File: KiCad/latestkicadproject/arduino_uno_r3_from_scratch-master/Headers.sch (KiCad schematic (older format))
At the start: 4 parts, among them P1 Power Header, P2 Analog Header, P3 Digital Header 02, P4 Digital Header 01

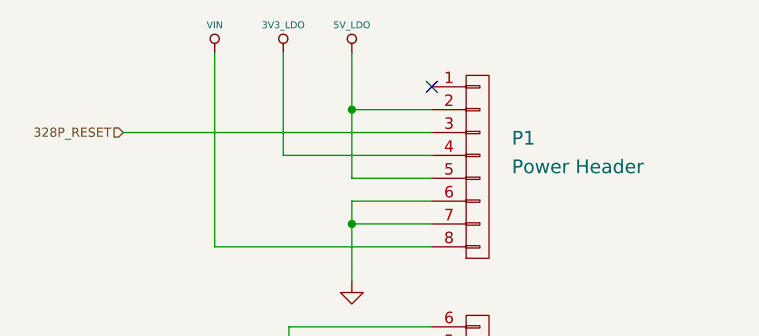
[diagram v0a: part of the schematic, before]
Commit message: 28feb
Aanpassing KiCad+deel footprints
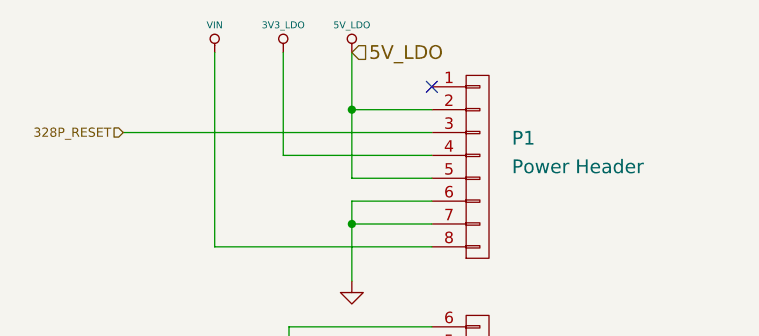
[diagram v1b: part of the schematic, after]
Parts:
- P1, P2, P3, P4: footprint ~ -> (none)
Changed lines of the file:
@@
 F 0 "P1" H 6400 2500 60  0000 L CNN
 F 1 "Power Header" H 6400 2375 60  0000 L CNN
-F 2 "~" H 6250 2375 60  0000 C CNN
+F 2 "" H 6250 2375 60  0000 C CNN
 F 3 "http://sullinscorp.com/catalogs/101_PAGE114-115_.100_FEMALE_HDR.pdf" H 6250 2375 60  0001 C CNN
 F 4 "Connector Header 8 Position 0.100\" (2.54mm) Gold Surface Mount" H 6250 2375 60  0001 C CNN "Characteristics"
@@
 F 0 "P3" H 6450 4250 60  0000 C CNN
 F 1 "Digital Header 02" H 6400 4375 60  0000 L CNN
-F 2 "~" H 6250 4375 60  0000 C CNN
+F 2 "" H 6250 4375 60  0000 C CNN
 F 3 "http://sullinscorp.com/catalogs/101_PAGE114-115_.100_FEMALE_HDR.pdf" H 6250 4375 60  0001 C CNN
 F 4 "Connector Header 10 Position 0.100\" (2.54mm) Gold Surface Mount" H 6250 4375 60  0001 C CNN "Characteristics"
@@
 F 0 "P2" H 6400 3200 60  0000 L CNN
 F 1 "Analog Header" H 6400 3325 60  0000 L CNN
-F 2 "~" H 6250 3325 60  0000 C CNN
+F 2 "" H 6250 3325 60  0000 C CNN
 F 3 "http://sullinscorp.com/catalogs/101_PAGE114-115_.100_FEMALE_HDR.pdf" H 6250 3325 60  0001 C CNN
 F 4 "Connector Header 6 Position 0.100\" (2.54mm) Gold Surface Mount" H 6250 3325 60  0001 C CNN "Characteristics"
@@
 F 0 "P4" H 6400 5650 60  0000 L CNN
 F 1 "Digital Header 01" H 6400 5525 60  0000 L CNN
-F 2 "~" H 6250 5525 60  0000 C CNN
+F 2 "" H 6250 5525 60  0000 C CNN
 F 3 "http://sullinscorp.com/catalogs/101_PAGE114-115_.100_FEMALE_HDR.pdf" H 6250 5525 60  0001 C CNN
 F 4 "Connector Header 8 Position 0.100\" (2.54mm) Gold Surface Mount" H 6250 5525 60  0001 C CNN "Characteristics"
@@
 	1    0    0    -1
 $EndComp
+Text HLabel 5700 1875 2    60   Input ~ 0
+5V_LDO
 $EndSCHEMATC

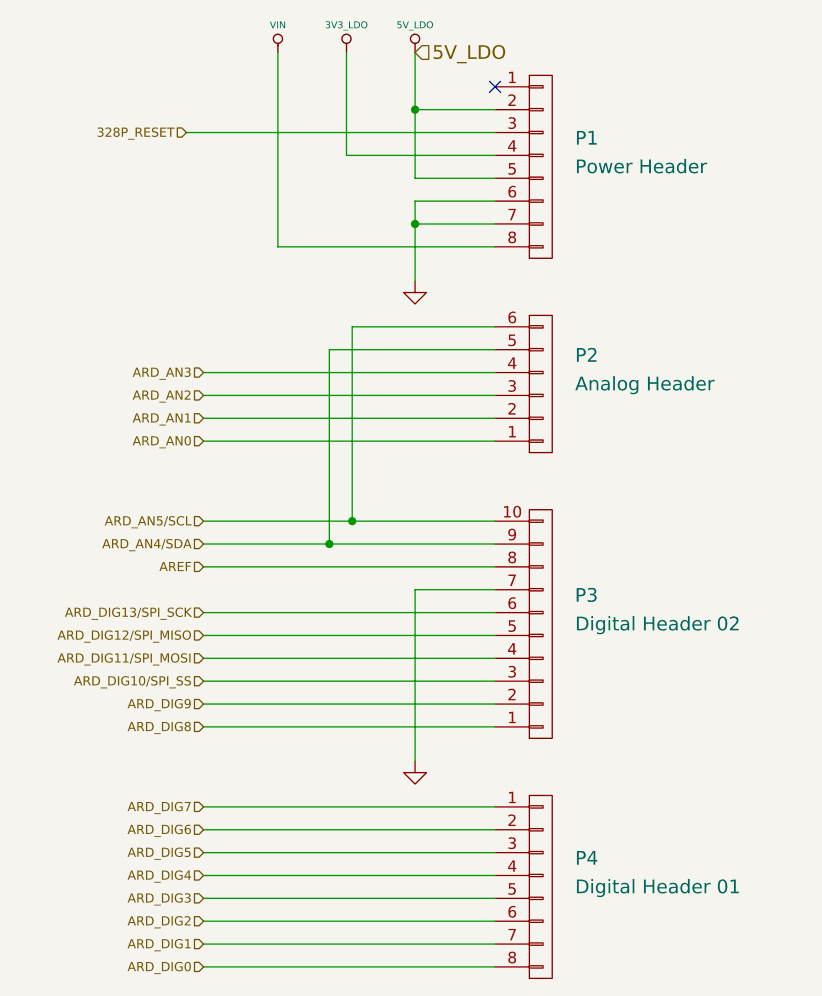
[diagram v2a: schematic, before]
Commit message: Aanpassing KiCad PCB ontwerp + footprints
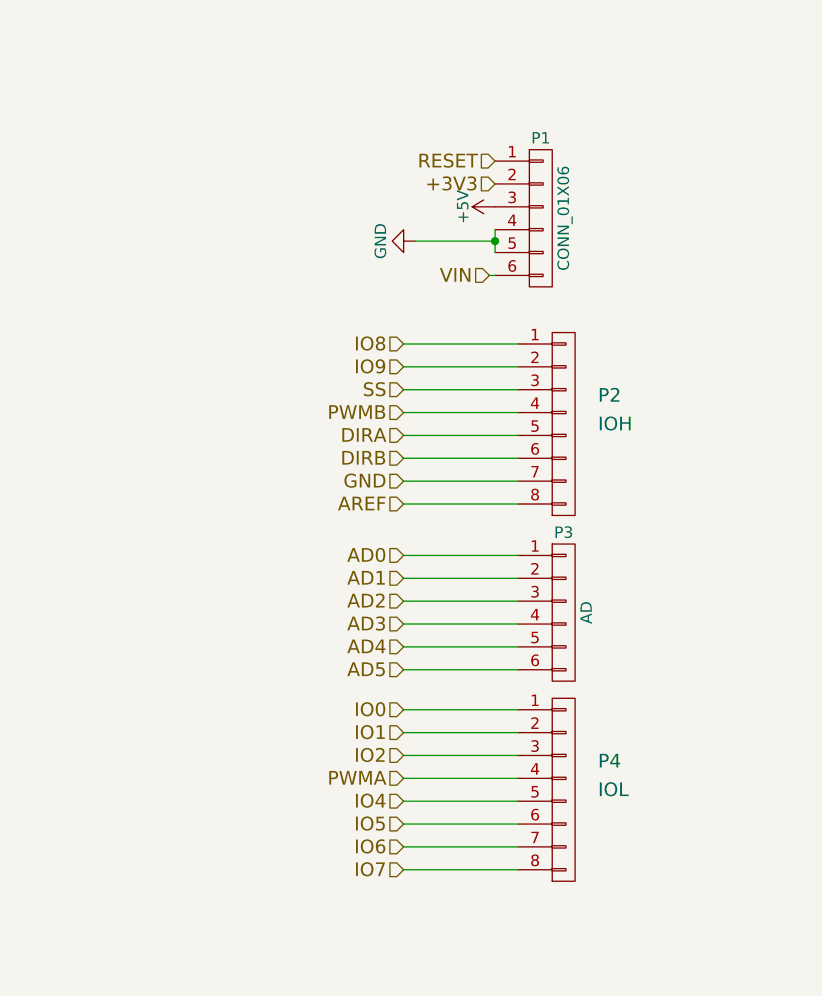
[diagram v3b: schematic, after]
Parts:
- removed P1: Power Header, symbol CONN_01X08
- removed P2: Analog Header, symbol CONN_01X06
- removed P3: Digital Header 02, symbol CONN_01X10
- added P1: CONN_01X06, Pin_Headers:Pin_Header_Straight_1x06_Pitch2.00mm, symbol CONN_01X06
- added P2: IOH, Pin_Headers:Pin_Header_Straight_1x08_Pitch2.00mm, symbol CONN_01X08
- added P3: AD, Pin_Headers:Pin_Header_Straight_1x06_Pitch2.00mm, symbol CONN_01X06
- P4: value Digital Header 01 -> IOL; footprint (none) -> Pin_Headers:Pin_Header_Straight_1x08_Pitch2.00mm
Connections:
- net AREF: now also P2.8 (P8)
- net ARD_DIG0 renamed IO7
- net ARD_DIG1 renamed IO6
- net ARD_DIG2 renamed IO5
- net ARD_DIG3 renamed IO4
- net ARD_DIG4 renamed PWMA
- net ARD_DIG5 renamed IO2
- net ARD_DIG6 renamed IO1
- net ARD_DIG7 renamed IO0
- new net +3V3: P1.2 (P2)
- new net +5V: P1.3 (P3)
- new net AD0: P3.1 (P1)
- new net AD1: P3.2 (P2)
- new net AD2: P3.3 (P3)
- new net AD3: P3.4 (P4)
- new net AD4: P3.5 (P5)
- new net AD5: P3.6 (P6)
- new net DIRA: P2.5 (P5)
- new net DIRB: P2.6 (P6)
- new net GND: P1.4 (P4), P1.5 (P5), P2.7 (P7)
- new net IO8: P2.1 (P1)
- new net IO9: P2.2 (P2)
- new net PWMB: P2.4 (P4)
- new net RESET: P1.1 (P1)
- new net SS: P2.3 (P3)
- new net VIN: P1.6 (P6)
- no-connect marks 1 -> 0
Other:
- moved on the sheet: P4

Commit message: pcb routing
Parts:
- P1, P3: footprint Pin_Headers:Pin_Header_Straight_1x06_Pitch2.00mm -> Pin_Headers:Pin_Header_Straight_1x06_Pitch2.54mm
- P2: footprint Pin_Headers:Pin_Header_Straight_1x08_Pitch2.00mm -> Pin_Headers:Pin_Header_Straight_1x08_Pitch2.54mm
- P4: value IOL -> H4; footprint Pin_Headers:Pin_Header_Straight_1x08_Pitch2.00mm -> Pin_Headers:Pin_Header_Straight_1x08_Pitch2.54mm
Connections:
- net +5V: now also P1.5 (P5); no longer P1.3 (P3)
- net AD0: now also P2.8 (P8); no longer P3.1 (P1)
- net AD1: now also P2.7 (P7); no longer P3.2 (P2)
- net AD2: now also P2.6 (P6); no longer P3.3 (P3)
- net AD3: now also P2.5 (P5); no longer P3.4 (P4)
- net AD4: now also P2.4 (P4); no longer P3.5 (P5)
- net AD5: now also P2.3 (P3); no longer P3.6 (P6)
- net AREF: now also P1.4 (P4); no longer P2.8 (P8)
- net DIRA: now also P4.8 (P8); no longer P2.5 (P5)
- net DIRB: now also P1.6 (P6); no longer P2.6 (P6)
- net GND: now also P1.3 (P3), P3.5 (P5), P3.6 (P6); no longer P1.4 (P4), P1.5 (P5), P2.7 (P7)
- net IO0: now also P2.1 (P1); no longer P4.1 (P1)
- net IO1: now also P3.1 (P1); no longer P4.2 (P2)
- net IO2: now also P3.2 (P2); no longer P4.3 (P3)
- net IO4: now also P3.4 (P4); no longer P4.5 (P5)
- net IO5: now also P4.1 (P1); no longer P4.6 (P6)
- net IO6: now also P4.2 (P2); no longer P4.7 (P7)
- net IO7: now also P4.3 (P3); no longer P4.8 (P8)
- net IO8: now also P4.4 (P4); no longer P2.1 (P1)
- net IO9: now also P4.5 (P5); no longer P2.2 (P2)
- net PWMA: now also P3.3 (P3); no longer P4.4 (P4)
- net PWMB: now also P4.7 (P7); no longer P2.4 (P4)
- net RESET: now also P2.2 (P2); no longer P1.1 (P1)
- net SS: now also P4.6 (P6); no longer P2.3 (P3)
- net VIN: now also P1.1 (P1); no longer P1.6 (P6)
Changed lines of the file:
@@
 LIBS:LP2985-33DBVR
 LIBS:degson
+LIBS:PHT6NQ10T_135
 EELAYER 25 0
 EELAYER END
@@
 P 6350 5100
 F 0 "P4" H 6500 5225 60  0000 L CNN
-F 1 "IOL" H 6500 5100 60  0000 L CNN
-F 2 "Pin_Headers:Pin_Header_Straight_1x08_Pitch2.00mm" H 6350 5100 60  0001 C CNN
+F 1 "H4" H 6500 5100 60  0000 L CNN
+F 2 "Pin_Headers:Pin_Header_Straight_1x08_Pitch2.54mm" H 6350 5100 60  0001 C CNN
 F 3 "http://sullinscorp.com/catalogs/101_PAGE114-115_.100_FEMALE_HDR.pdf" H 6350 5100 60  0001 C CNN
 F 4 "Connector Header 8 Position 0.100\" (2.54mm) Gold Surface Mount" H 6350 5100 60  0001 C CNN "Characteristics"
@@
 Text HLabel 6050 2450 0    60   Input ~ 0
 +3V3
-Text HLabel 6025 2850 0    60   Input ~ 0
+Text HLabel 6050 2350 0    60   Input ~ 0
 VIN
-Text HLabel 6050 2350 0    60   Input ~ 0
+Text HLabel 5650 3250 0    60   Input ~ 0
 RESET
 $Comp
@@
 F 0 "P1" H 6250 2950 50  0000 C CNN
 F 1 "CONN_01X06" V 6350 2600 50  0000 C CNN
-F 2 "Pin_Headers:Pin_Header_Straight_1x06_Pitch2.00mm" H 6250 2600 60  0001 C CNN
+F 2 "Pin_Headers:Pin_Header_Straight_1x06_Pitch2.54mm" H 6250 2600 60  0001 C CNN
 F 3 "" H 6250 2600 60  0000 C CNN
 	1    6250 2600
@@
 L +5V #PWR09
 U 1 1 5AA11396
+P 6050 2750
+F 0 "#PWR09" H 6050 2600 50  0001 C CNN
+F 1 "+5V" H 6050 2890 50  0000 C CNN
+F 2 "" H 6050 2750 50  0001 C CNN
+F 3 "" H 6050 2750 50  0001 C CNN
+	1    6050 2750
+	0    -1   -1   0
+$EndComp
+$Comp
+L GND #PWR010
+U 1 1 5AA115CD
 P 6050 2550
-F 0 "#PWR09" H 6050 2400 50  0001 C CNN
-F 1 "+5V" H 6050 2690 50  0000 C CNN
+F 0 "#PWR010" H 6050 2300 50  0001 C CNN
+F 1 "GND" H 6050 2400 50  0000 C CNN
 F 2 "" H 6050 2550 50  0001 C CNN
 F 3 "" H 6050 2550 50  0001 C CNN
 	1    6050 2550
-	0    -1   -1   0
-$EndComp
-Wire Wire Line
-	6050 2750 6050 2650
-Wire Wire Line
-	6050 2700 5700 2700
-Connection ~ 6050 2700
-$Comp
-L GND #PWR010
-U 1 1 5AA115CD
-P 5700 2700
-F 0 "#PWR010" H 5700 2450 50  0001 C CNN
-F 1 "GND" H 5700 2550 50  0000 C CNN
-F 2 "" H 5700 2700 50  0001 C CNN
-F 3 "" H 5700 2700 50  0001 C CNN
-	1    5700 2700
 	0    1    1    0
 $EndComp
@@
 F 0 "P2" H 6500 3625 60  0000 L CNN
 F 1 "IOH" H 6500 3500 60  0000 L CNN
-F 2 "Pin_Headers:Pin_Header_Straight_1x08_Pitch2.00mm" H 6350 3500 60  0001 C CNN
+F 2 "Pin_Headers:Pin_Header_Straight_1x08_Pitch2.54mm" H 6350 3500 60  0001 C CNN
 F 3 "http://sullinscorp.com/catalogs/101_PAGE114-115_.100_FEMALE_HDR.pdf" H 6350 3500 60  0001 C CNN
 F 4 "Connector Header 8 Position 0.100\" (2.54mm) Gold Surface Mount" H 6350 3500 60  0001 C CNN "Characteristics"
@@
 F 0 "P3" H 6350 4675 50  0000 C CNN
 F 1 "AD" V 6450 4325 50  0000 C CNN
-F 2 "Pin_Headers:Pin_Header_Straight_1x06_Pitch2.00mm" H 6350 4325 60  0001 C CNN
+F 2 "Pin_Headers:Pin_Header_Straight_1x06_Pitch2.54mm" H 6350 4325 60  0001 C CNN
 F 3 "" H 6350 4325 60  0000 C CNN
 	1    6350 4325
@@
 Wire Wire Line
 	6150 5450 5650 5450
+Text HLabel 5650 5050 0    60   Input ~ 0
+IO8
+Text HLabel 5650 5150 0    60   Input ~ 0
+IO9
+Text HLabel 5650 5250 0    60   Input ~ 0
+SS
+Text HLabel 5650 5350 0    60   Input ~ 0
+PWMB
+Text HLabel 5650 5450 0    60   Input ~ 0
+DIRA
+Text HLabel 6025 2850 0    60   Input ~ 0
+DIRB
+Text HLabel 5650 4475 0    60   Input ~ 0
+GND
+Text HLabel 6050 2650 0    60   Input ~ 0
+AREF
+Text HLabel 5650 3850 0    60   Input ~ 0
+AD0
+Text HLabel 5650 3750 0    60   Input ~ 0
+AD1
+Text HLabel 5650 3650 0    60   Input ~ 0
+AD2
+Text HLabel 5650 3550 0    60   Input ~ 0
+AD3
+Text HLabel 5650 3450 0    60   Input ~ 0
+AD4
+Text HLabel 5650 3350 0    60   Input ~ 0
+AD5
+Text HLabel 5650 4075 0    60   Input ~ 0
+IO1
 Text HLabel 5650 3150 0    60   Input ~ 0
-IO8
-Text HLabel 5650 3250 0    60   Input ~ 0
-IO9
-Text HLabel 5650 3350 0    60   Input ~ 0
-SS
-Text HLabel 5650 3450 0    60   Input ~ 0
-PWMB
-Text HLabel 5650 3550 0    60   Input ~ 0
-DIRA
-Text HLabel 5650 3650 0    60   Input ~ 0
-DIRB
-Text HLabel 5650 3750 0    60   Input ~ 0
+IO0
+Text HLabel 5650 4175 0    60   Input ~ 0
+IO2
+Text HLabel 5650 4275 0    60   Input ~ 0
+PWMA
+Text HLabel 5650 4375 0    60   Input ~ 0
+IO4
+Text HLabel 5650 4750 0    60   Input ~ 0
+IO5
+Text HLabel 5650 4850 0    60   Input ~ 0
+IO6
+Text HLabel 5650 4950 0    60   Input ~ 0
+IO7
+Wire Wire Line
+	6025 2850 6050 2850
+Text HLabel 5650 4575 0    60   Input ~ 0
 GND
-Text HLabel 5650 3850 0    60   Input ~ 0
-AREF
-Text HLabel 5650 4075 0    60   Input ~ 0
-AD0
-Text HLabel 5650 4175 0    60   Input ~ 0
-AD1
-Text HLabel 5650 4275 0    60   Input ~ 0
-AD2
-Text HLabel 5650 4375 0    60   Input ~ 0
-AD3
-Text HLabel 5650 4475 0    60   Input ~ 0
-AD4
-Text HLabel 5650 4575 0    60   Input ~ 0
-AD5
-Text HLabel 5650 4850 0    60   Input ~ 0
-IO1
-Text HLabel 5650 4750 0    60   Input ~ 0
-IO0
-Text HLabel 5650 4950 0    60   Input ~ 0
-IO2
-Text HLabel 5650 5050 0    60   Input ~ 0
-PWMA
-Text HLabel 5650 5150 0    60   Input ~ 0
-IO4
-Text HLabel 5650 5250 0    60   Input ~ 0
-IO5
-Text HLabel 5650 5350 0    60   Input ~ 0
-IO6
-Text HLabel 5650 5450 0    60   Input ~ 0
-IO7
-Wire Wire Line
-	6025 2850 6050 2850
 $EndSCHEMATC

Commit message: PCB routing v1
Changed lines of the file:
@@
 LIBS:degson
 LIBS:PHT6NQ10T_135
+LIBS:L298P
 EELAYER 25 0
 EELAYER END
@@
 Text HLabel 6025 2850 0    60   Input ~ 0
 DIRB
-Text HLabel 5650 4475 0    60   Input ~ 0
-GND
 Text HLabel 6050 2650 0    60   Input ~ 0
 AREF
@@
 Wire Wire Line
 	6025 2850 6050 2850
-Text HLabel 5650 4575 0    60   Input ~ 0
+$Comp
+L GND #PWR011
+U 1 1 5AB3A500
+P 5650 4575
+F 0 "#PWR011" H 5650 4325 50  0001 C CNN
+F 1 "GND" H 5650 4425 50  0000 C CNN
+F 2 "" H 5650 4575 50  0001 C CNN
+F 3 "" H 5650 4575 50  0001 C CNN
+	1    5650 4575
+	1    0    0    -1
+$EndComp
+$Comp
+L GND #PWR012
+U 1 1 5AB3A534
+P 5650 4475
+F 0 "#PWR012" H 5650 4225 50  0001 C CNN
+F 1 "GND" H 5650 4325 50  0000 C CNN
+F 2 "" H 5650 4475 50  0001 C CNN
+F 3 "" H 5650 4475 50  0001 C CNN
+	1    5650 4475
+	1    0    0    -1
+$EndComp
+Text HLabel 5050 2500 0    60   Input ~ 0
 GND
+$Comp
+L GND #PWR013
+U 1 1 5AB75FDA
+P 5050 2500
+F 0 "#PWR013" H 5050 2250 50  0001 C CNN
+F 1 "GND" H 5050 2350 50  0000 C CNN
+F 2 "" H 5050 2500 50  0001 C CNN
+F 3 "" H 5050 2500 50  0001 C CNN
+	1    5050 2500
+	1    0    0    -1
+$EndComp
 $EndSCHEMATC

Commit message: verbeteringen kicad
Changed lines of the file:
@@
-$EndComp
-$Comp
-L GND #PWR06
-U 1 1 5AA115CD
-P 6050 2550
-F 0 "#PWR06" H 6050 2300 50  0001 C CNN
-F 1 "GND" H 6050 2400 50  0000 C CNN
-F 2 "" H 6050 2550 50  0001 C CNN
-F 3 "" H 6050 2550 50  0001 C CNN
-	1    6050 2550
-	0    1    1    0
 $EndComp
 $Comp
@@
 Wire Wire Line
 	6025 2850 6050 2850
-$Comp
-L GND #PWR07
-U 1 1 5AB3A500
-P 5650 4575
-F 0 "#PWR07" H 5650 4325 50  0001 C CNN
-F 1 "GND" H 5650 4425 50  0000 C CNN
-F 2 "" H 5650 4575 50  0001 C CNN
-F 3 "" H 5650 4575 50  0001 C CNN
-	1    5650 4575
-	1    0    0    -1
-$EndComp
-$Comp
-L GND #PWR08
-U 1 1 5AB3A534
-P 5650 4475
-F 0 "#PWR08" H 5650 4225 50  0001 C CNN
-F 1 "GND" H 5650 4325 50  0000 C CNN
-F 2 "" H 5650 4475 50  0001 C CNN
-F 3 "" H 5650 4475 50  0001 C CNN
-	1    5650 4475
-	1    0    0    -1
-$EndComp
-Text HLabel 5050 2500 0    60   Input ~ 0
+Text HLabel 6050 2550 0    60   Input ~ 0
 GND
-$Comp
-L GND #PWR09
-U 1 1 5AB75FDA
-P 5050 2500
-F 0 "#PWR09" H 5050 2250 50  0001 C CNN
-F 1 "GND" H 5050 2350 50  0000 C CNN
-F 2 "" H 5050 2500 50  0001 C CNN
-F 3 "" H 5050 2500 50  0001 C CNN
-	1    5050 2500
-	1    0    0    -1
-$EndComp
+Text HLabel 5650 4475 0    60   Input ~ 0
+GND
+Text HLabel 5650 4575 0    60   Input ~ 0
+GND
 $EndSCHEMATC
